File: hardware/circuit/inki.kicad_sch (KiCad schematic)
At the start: 52 parts, among them J1 connector epaper, J2 Conn_01x02_Socket, J3 Conn_01x02_Socket, J4 Conn_01x02_Socket, J5 Conn_01x02_Socket, J7 Conn_01x02_Socket, Q1 TSM260P02CX, Q2 MMBT3904, Q3 TSM260P02CX, Q4 MMBT3904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

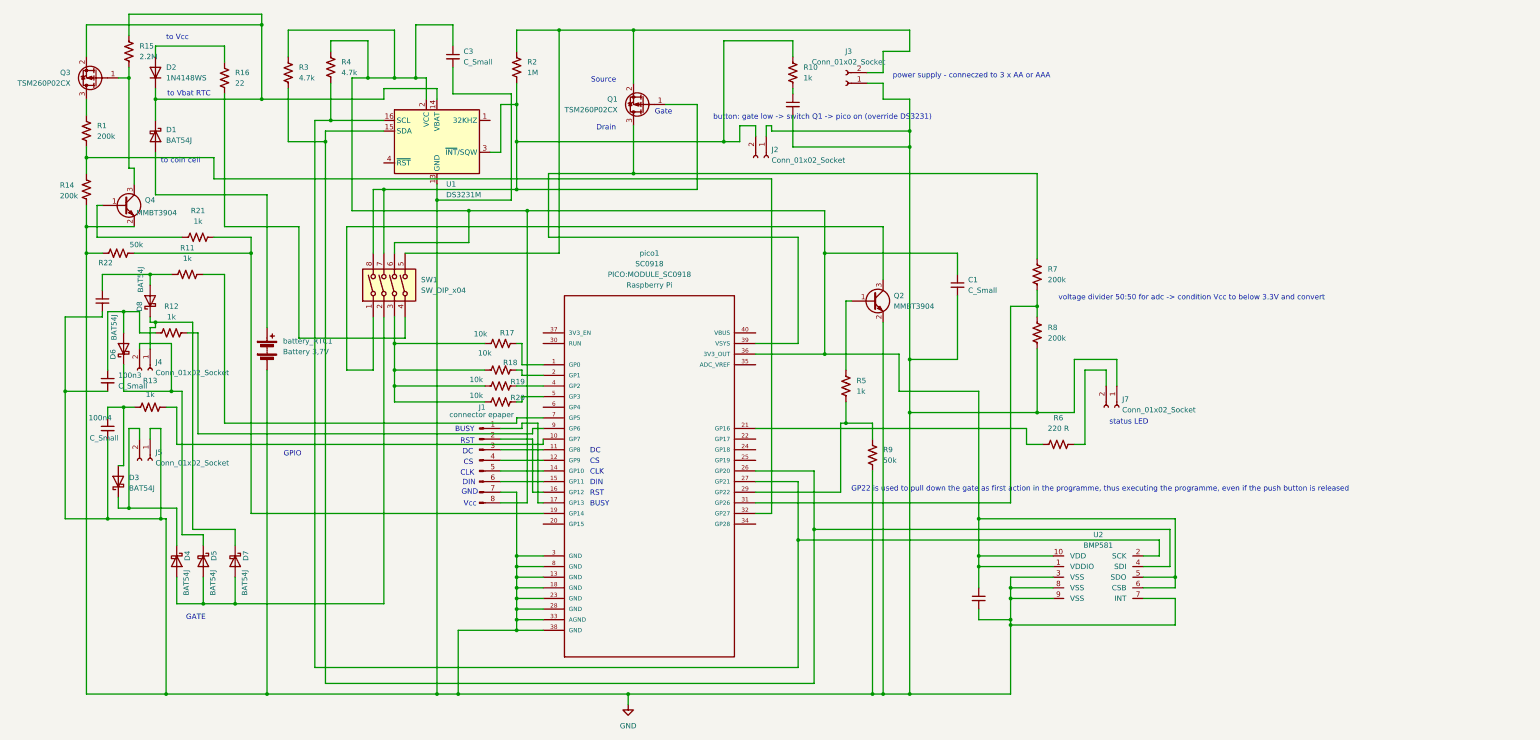
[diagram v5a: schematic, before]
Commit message: updated pcb, unified part names, added BOM
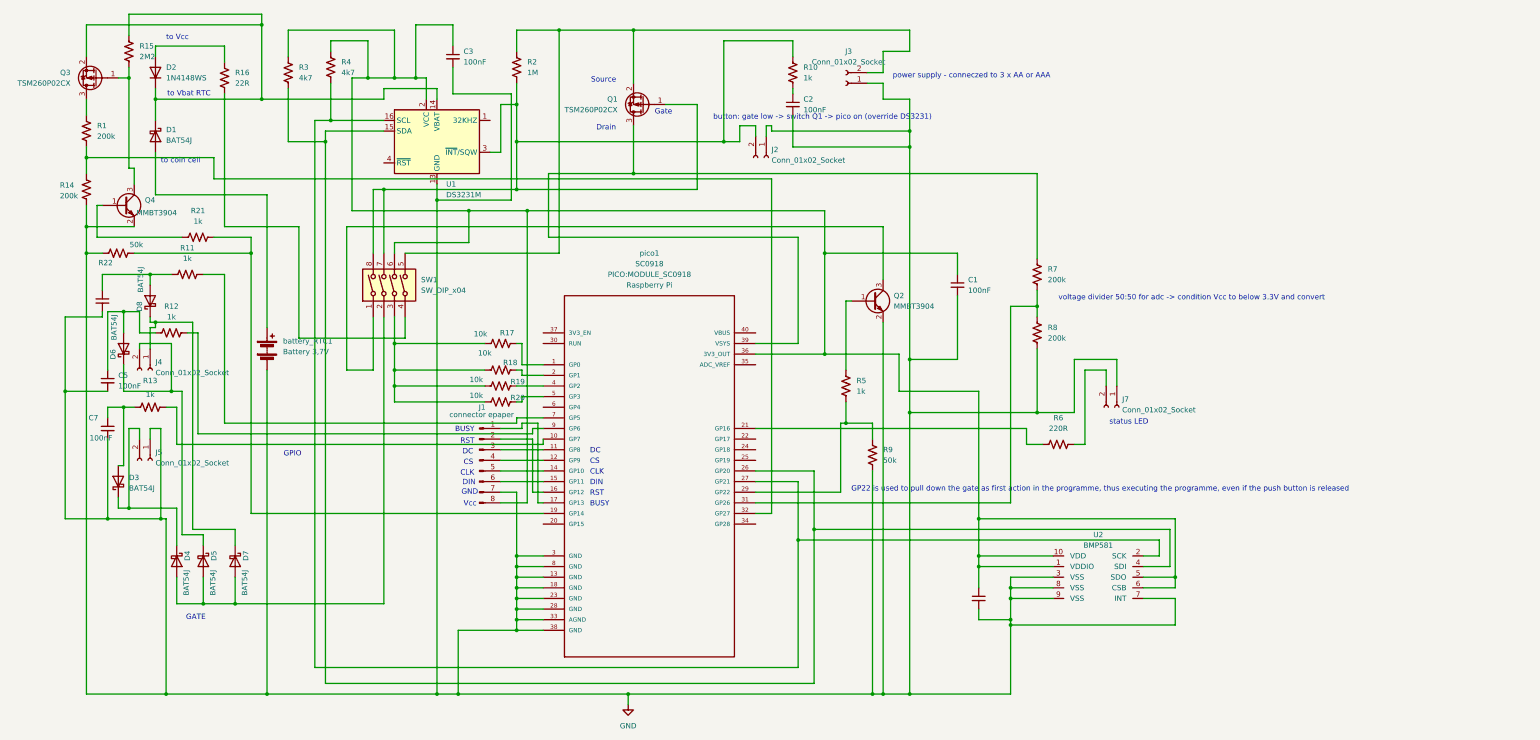
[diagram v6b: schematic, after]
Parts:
- C1, C3: value C_Small -> 100nF
- C2: renamed from 100n1; value C_Small -> 100nF
- C4: renamed from 100n2; value C_Small -> 100nF
- C5: renamed from 100n3; value C_Small -> 100nF
- C6: renamed from 100n5; value C_Small -> 100nF
- C7: renamed from 100n4; value C_Small -> 100nF
- R15: value 2.2M -> 2M2
- R16: value 22 -> 22R
- R3, R4: value 4.7k -> 4k7
- R6: value 220 R -> 220R

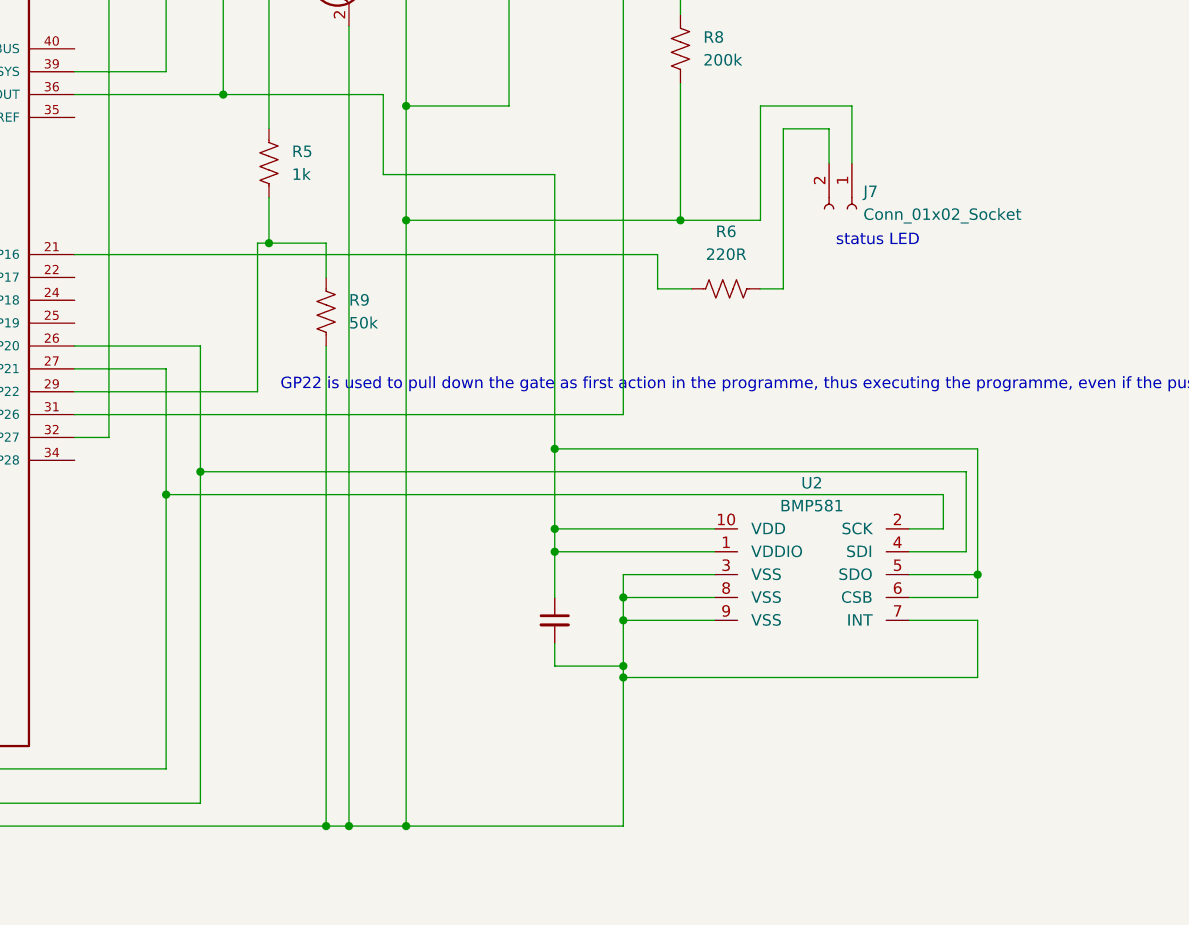
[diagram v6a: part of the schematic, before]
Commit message: add optional i2c sensor sheet and align bom values
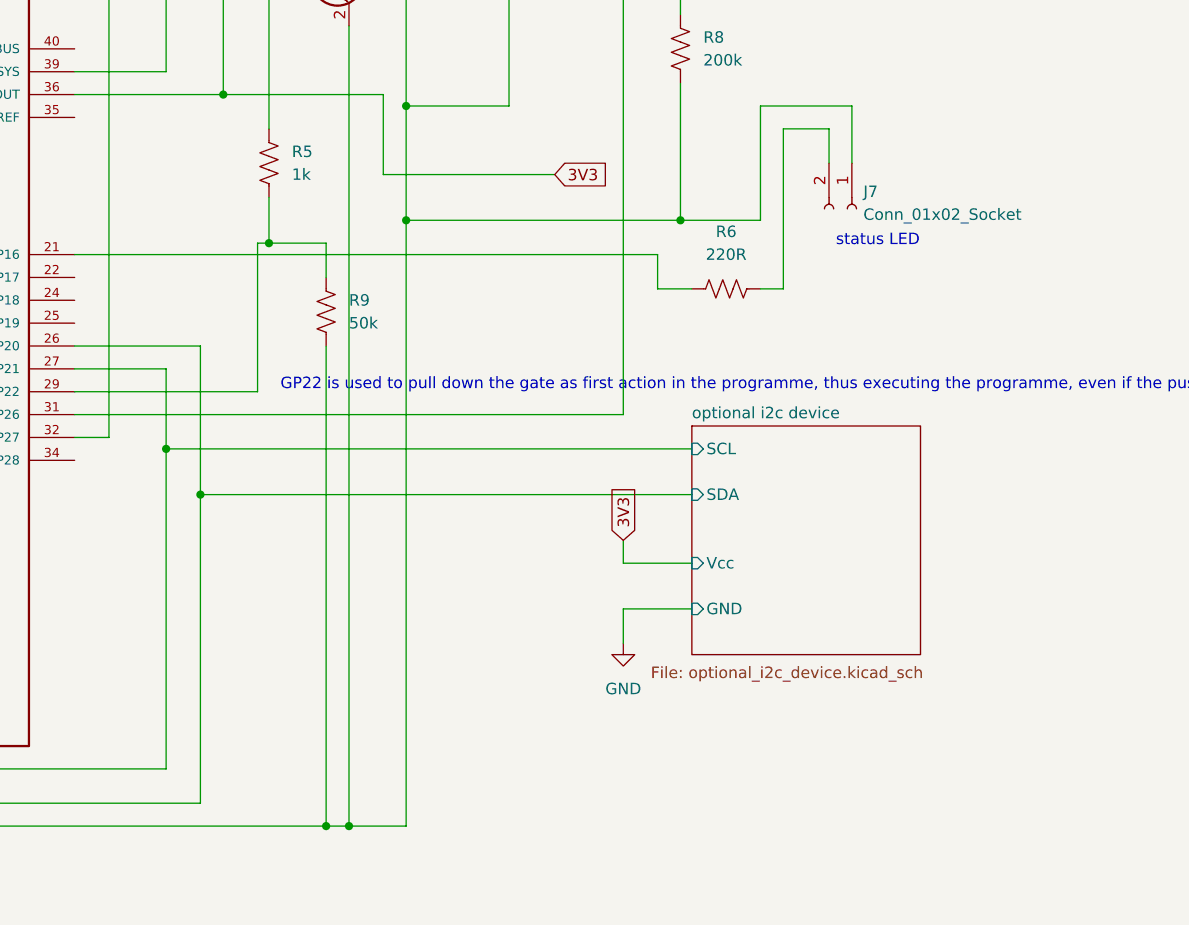
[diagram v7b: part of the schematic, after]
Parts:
- removed C6: 100nF, Capacitor_SMD:C_0805_2012Metric, symbol Device:C_Small
- removed U2: BMP581, inki:BMP581, symbol BMP581:BMP581
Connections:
- net optional i2c device/SDA: now reaches R3.2, U1.15 (SDA), pico1.26 (GP20)
- net optional i2c device/SCL: now reaches R4.2, U1.16 (SCL), pico1.27 (GP21)
- net 3V3: now reaches C1.1, C3.1, J1.8 (Pin_8), R3.1, R4.1, SW1.6, U1.2 (VCC), pico1.36 (3V3_OUT)
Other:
- added sheet optional i2c device (optional_i2c_device.kicad_sch)

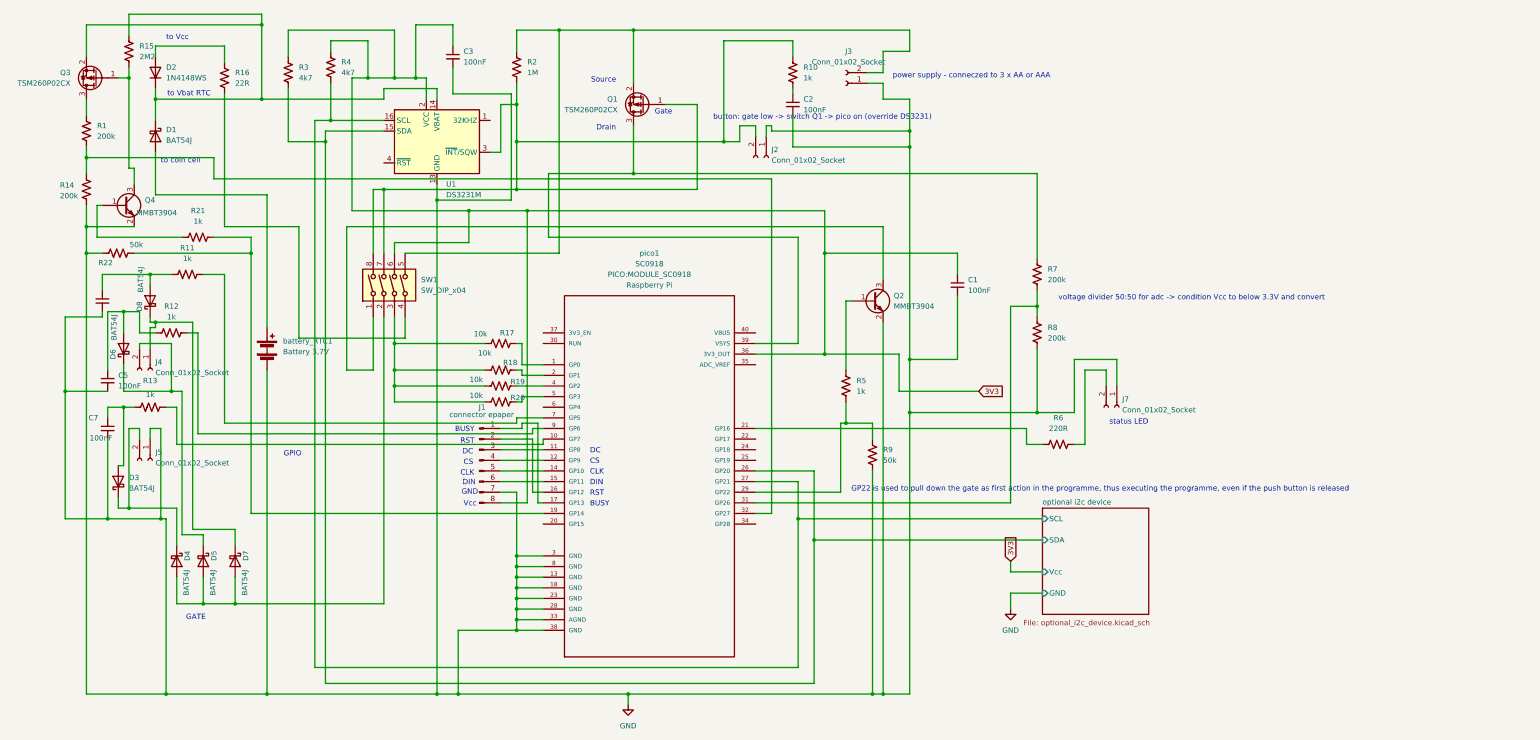
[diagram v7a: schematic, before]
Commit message: added optional i2c device, added gerber files - not tested! Use with care!
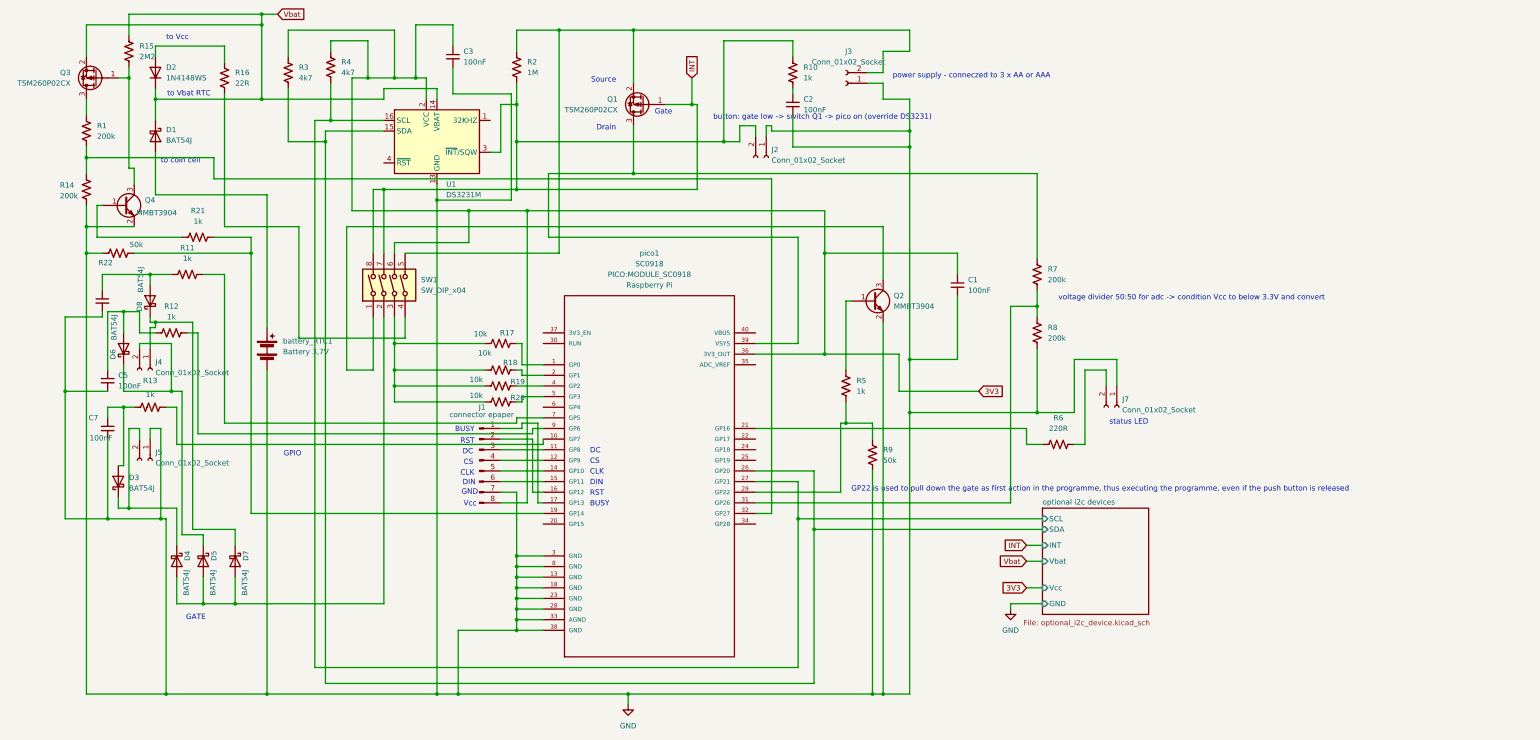
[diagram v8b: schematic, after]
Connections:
- net INT: now reaches J2.2 (Pin_2), Q1.1 (G), R10.2, R2.2, SW1.7, SW1.8, U1.3 (~{INT}/SQW)
- net Vbat: now reaches D1.1 (K), D2.1 (K), Q3.2 (S), R15.1, U1.14 (VBAT)
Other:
- sheet optional i2c device renamed optional i2c devices
- sheet optional i2c devices ports: added INT, Vbat; removed none
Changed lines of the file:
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@@
 	)
 	(junction
+		(at 59.69 15.24)
+		(diameter 0)
+		(color 0 0 0 0)
+	)
+	(junction
 		(at 205.74 177.8)
 		(diameter 0)
@@
 	)
 	(junction
-		(at 191.77 140.97)
+		(at 120.65 57.15)
 		(diameter 0)
 		(color 0 0 0 0)
 	)
 	(junction
-		(at 120.65 57.15)
+		(at 191.77 138.43)
 		(diameter 0)
 		(color 0 0 0 0)
@@
 	)
 	(junction
+		(at 162.56 36.83)
+		(diameter 0)
+		(color 0 0 0 0)
+	)
+	(junction
 		(at 26.67 86.36)
 		(diameter 0)
@@
 	(wire
 		(pts
-			(xy 191.77 140.97) (xy 246.38 140.97)
+			(xy 191.77 138.43) (xy 246.38 138.43)
 		)
 		(stroke
@@
 	(wire
 		(pts
+			(xy 162.56 30.48) (xy 162.56 36.83)
+		)
+		(stroke
+			(width 0)
+			(type default)
+		)
+	)
+	(wire
+		(pts
 			(xy 96.52 17.78) (xy 96.52 30.48)
 		)
@@
 	(wire
 		(pts
+			(xy 59.69 15.24) (xy 63.5 15.24)
+		)
+		(stroke
+			(width 0)
+			(type default)
+		)
+	)
+	(wire
+		(pts
 			(xy 36.83 135.89) (xy 36.83 177.8)
 		)
@@
 	(wire
 		(pts
-			(xy 238.76 146.05) (xy 238.76 148.59)
+			(xy 125.73 113.03) (xy 121.92 113.03)
 		)
 		(stroke
@@
 	(wire
 		(pts
-			(xy 125.73 113.03) (xy 121.92 113.03)
+			(xy 173.99 41.91) (xy 177.8 41.91)
 		)
 		(stroke
@@
 	(wire
 		(pts
-			(xy 173.99 41.91) (xy 177.8 41.91)
+			(xy 113.03 107.95) (xy 91.44 107.95)
 		)
 		(stroke
@@
 	(wire
 		(pts
-			(xy 113.03 107.95) (xy 91.44 107.95)
+			(xy 242.57 142.24) (xy 246.38 142.24)
 		)
 		(stroke
@@
 	(wire
 		(pts
-			(xy 191.77 140.97) (xy 191.77 175.26)
+			(xy 191.77 138.43) (xy 191.77 175.26)
 		)
 		(stroke
@@
 	(wire
 		(pts
-			(xy 238.76 153.67) (xy 238.76 157.48)
+			(xy 238.76 156.21) (xy 238.76 157.48)
 		)
 		(stroke
@@
 	(wire
 		(pts
-			(xy 246.38 148.59) (xy 238.76 148.59)
+			(xy 246.38 152.4) (xy 242.57 152.4)
 		)
 		(stroke
@@
 	(wire
 		(pts
+			(xy 242.57 146.05) (xy 246.38 146.05)
+		)
+		(stroke
+			(width 0)
+			(type default)
+		)
+	)
+	(wire
+		(pts
 			(xy 44.45 115.57) (xy 44.45 91.44)
 		)
@@
 	(wire
 		(pts
-			(xy 191.77 124.46) (xy 191.77 140.97)
+			(xy 191.77 124.46) (xy 191.77 138.43)
 		)
 		(stroke
@@
 	(wire
 		(pts
-			(xy 156.21 36.83) (xy 163.83 36.83)
+			(xy 156.21 36.83) (xy 162.56 36.83)
 		)
 		(stroke
@@
 	(wire
 		(pts
+			(xy 162.56 36.83) (xy 163.83 36.83)
+		)
+		(stroke
+			(width 0)
+			(type default)
+		)
+	)
+	(wire
+		(pts
 			(xy 163.83 36.83) (xy 163.83 57.15)
 		)
@@
 	(wire
 		(pts
-			(xy 246.38 153.67) (xy 238.76 153.67)
+			(xy 246.38 156.21) (xy 238.76 156.21)
 		)
 		(stroke
@@
 	(global_label "3V3"
 		(shape input)
-		(at 238.76 146.05 90)
+		(at 242.57 152.4 180)
 		(fields_autoplaced yes)
 		(effects
@@
 				(size 1.27 1.27)
 			)
-			(justify left)
+			(justify right)
 		)
 		(property "Intersheetrefs" "${INTERSHEET_REFS}"
-			(at 238.76 139.5572 90)
+			(at 236.0772 152.4 0)
 			(effects
 				(font
 					(size 1.27 1.27)
 				)
-				(justify left)
+				(justify right)
+				(hide yes)
+			)
+		)
+	)
+	(global_label "INT"
+		(shape input)
+		(at 242.57 142.24 180)
+		(fields_autoplaced yes)
+		(effects
+			(font
+				(size 1.27 1.27)
+			)
+			(justify right)
+		)
+		(property "Intersheetrefs" "${INTERSHEET_REFS}"
+			(at 236.6819 142.24 0)
+			(effects
+				(font
+					(size 1.27 1.27)
+				)
+				(justify right)
 				(hide yes)
 			)
@@
 		)
 	)
+	(global_label "Vbat"
+		(shape input)
+		(at 242.57 146.05 180)
+		(fields_autoplaced yes)
+		(effects
+			(font
+				(size 1.27 1.27)
+			)
+			(justify right)
+		)
+		(property "Intersheetrefs" "${INTERSHEET_REFS}"
+			(at 235.4725 146.05 0)
+			(effects
+				(font
+					(size 1.27 1.27)
+				)
+				(justify right)
+				(hide yes)
+			)
+		)
+	)
+	(global_label "Vbat"
+		(shape input)
+		(at 63.5 15.24 0)
+		(fields_autoplaced yes)
+		(effects
+			(font
+				(size 1.27 1.27)
+			)
+			(justify left)
+		)
+		(property "Intersheetrefs" "${INTERSHEET_REFS}"
+			(at 70.5975 15.24 0)
+			(effects
+				(font
+					(size 1.27 1.27)
+				)
+				(justify left)
+				(hide yes)
+			)
+		)
+	)
+	(global_label "INT"
+		(shape input)
+		(at 162.56 30.48 90)
+		(fields_autoplaced yes)
+		(effects
+			(font
+				(size 1.27 1.27)
+			)
+			(justify left)
+		)
+		(property "Intersheetrefs" "${INTERSHEET_REFS}"
+			(at 162.56 24.5919 90)
+			(effects
+				(font
+					(size 1.27 1.27)
+				)
+				(justify left)
+				(hide yes)
+			)
+		)
+	)
 	(symbol
 		(lib_id "Device:R_US")
@@
 			(color 0 0 0 0.0000)
 		)
-		(property "Sheetname" "optional i2c device"
+		(property "Sheetname" "optional i2c devices"
 			(at 246.38 132.6384 0)
 			(effects
@@
 		)
 		(pin "SDA" input
-			(at 246.38 140.97 180)
+			(at 246.38 138.43 180)
 			(effects
 				(font
@@
 		)
 		(pin "Vcc" input
-			(at 246.38 148.59 180)
+			(at 246.38 152.4 180)
 			(effects
 				(font
@@
 		)
 		(pin "GND" input
-			(at 246.38 153.67 180)
+			(at 246.38 156.21 180)
+			(effects
+				(font
+					(size 1.27 1.27)
+				)
+				(justify left)
+			)
+		)
+		(pin "INT" input
+			(at 246.38 142.24 180)
+			(effects
+				(font
+					(size 1.27 1.27)
+				)
+				(justify left)
+			)
+		)
+		(pin "Vbat" input
+			(at 246.38 146.05 180)
 			(effects
 				(font
